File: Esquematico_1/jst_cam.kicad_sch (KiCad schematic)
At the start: 10 parts, among them J1 Screw_Terminal_01x04, J2 Screw_Terminal_01x03, J3 Screw_Terminal_01x06, J4 Screw_Terminal_01x08, J5 USB_C_Receptacle_USB2.0_14P, J6 Screw_Terminal_01x05, J7 Screw_Terminal_01x02, U5 USBLC6-2SC6

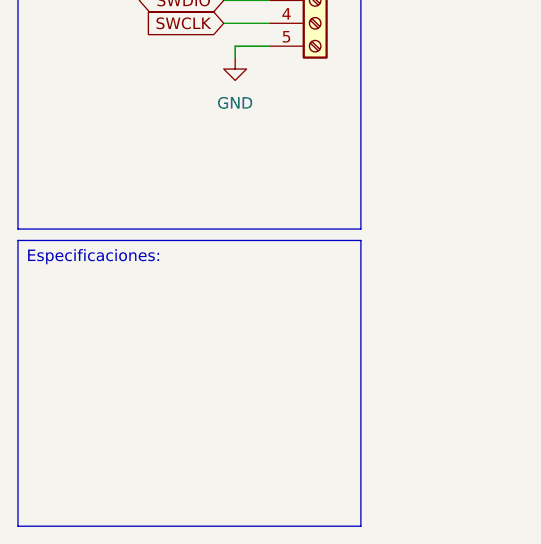
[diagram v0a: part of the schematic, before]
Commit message: Update Circuito de medicion de bateria
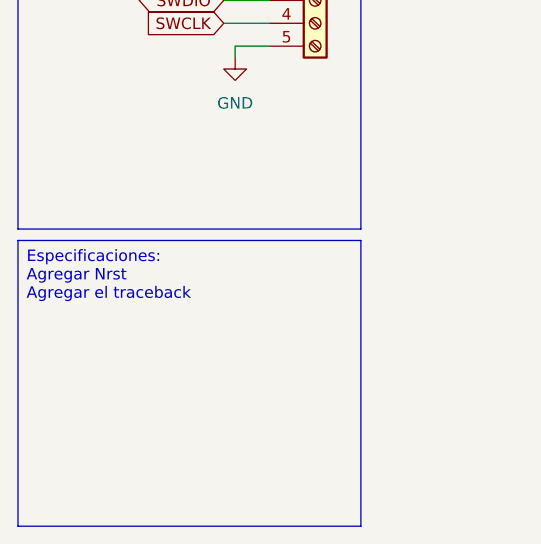
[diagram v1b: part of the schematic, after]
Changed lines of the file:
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@@
 		)
 	)
-	(text_box "Especificaciones: "
+	(text_box "Especificaciones: \nAgregar Nrst\nAgregar el traceback\n"
 		(exclude_from_sim no)
 		(at 24.13 149.86 0)

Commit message: último sensor conectado, y le quité los colores al net_signal xdd
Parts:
- added D3: D_Schottky, symbol Device:D_Schottky
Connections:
- net at J5.A4 (VBUS), J5.A9 (VBUS), J5.B4 (VBUS)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: now also D3.2 (A); no longer U5.5 (VBUS)
- new net: D3.1 (K), U5.5 (VBUS)
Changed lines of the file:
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@@
-	(wire
-		(pts
-			(xy 124.46 113.03) (xy 139.7 113.03)
-		)
-		(stroke
-			(width 0)
-			(type default)
-		)
-	)
 	(wire
 		(pts
@@
 	(wire
 		(pts
+			(xy 137.16 113.03) (xy 139.7 113.03)
+		)
+		(stroke
+			(width 0)
+			(type default)
+		)
+	)
+	(wire
+		(pts
 			(xy 52.07 115.57) (xy 52.07 118.11)
 		)
@@
 		(pts
 			(xy 190.5 46.99) (xy 194.31 46.99)
+		)
+		(stroke
+			(width 0)
+			(type default)
+		)
+	)
+	(wire
+		(pts
+			(xy 124.46 113.03) (xy 129.54 113.03)
 		)
 		(stroke
@@
 					(unit 1)
 				)
+			)
+		)
+	)
+	(symbol
+		(lib_id "Device:D_Schottky")
+		(at 133.35 113.03 180)
+		(unit 1)
+		(exclude_from_sim no)
+		(in_bom yes)
+		(on_board yes)
+		(dnp no)
+		(fields_autoplaced yes)
+		(property "Reference" "D3"
+			(at 133.6675 106.68 0)
+			(effects
+				(font
+					(size 1.27 1.27)
+				)
+			)
+		)
+		(property "Value" "D_Schottky"
+			(at 133.6675 109.22 0)
+			(effects
+				(font
+					(size 1.27 1.27)
+				)
+			)
+		)
+		(property "Footprint" ""
+			(at 133.35 113.03 0)
+			(effects
+				(font
+					(size 1.27 1.27)
+				)
+				(hide yes)
+			)
+		)
+		(property "Datasheet" "~"
+			(at 133.35 113.03 0)
+			(effects
+				(font
+					(size 1.27 1.27)
+				)
+				(hide yes)
+			)
+		)
+		(property "Description" "Schottky diode"
+			(at 133.35 113.03 0)
+			(effects
+				(font
+					(size 1.27 1.27)
+				)
+				(hide yes)
+			)
+		)
+		(pin "1"
+		)
+		(pin "2"
+		)
+		(instances
+			(project ""
+				(path "/de2d80c1-c21c-478d-b724-17659b714c38/457e76de-adfe-4ec5-a818-c5970caa89a7"
+					(reference "D3")
+					(unit 1)
+				)

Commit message: Update llamada
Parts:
- removed J7: Screw_Terminal_01x02, symbol Connector:Screw_Terminal_01x02
- added D4, D5, D6: D_Schottky, symbol Device:D_Schottky
- added JP1, JP2: SolderJumper_2_Open, symbol Jumper:SolderJumper_2_Open
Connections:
- net 5v: now also D4.2 (A), D5.2 (A), D6.2 (A); no longer J1.3 (Pin_3), J2.1 (Pin_1), J3.4 (Pin_4)
- net ESC1: now also J4.1 (Pin_1)
- net ESC2: now also J4.2 (Pin_2)
- net ESC3: now also J4.3 (Pin_3)
- net ESC4: now also J4.4 (Pin_4)
- net TELEM_ESC: now also J4.6 (Pin_6)
- net at J4.5 (Pin_5): now also JP2.1 (A)
- net at J4.7 (Pin_7): now also JP1.1 (A)
- new net: D5.1 (K), J1.3 (Pin_3)
- new net: D6.1 (K), J2.1 (Pin_1)
- new net: D4.1 (K), J3.4 (Pin_4)
- new net CRT: JP2.2 (B)
- new net VCC: JP1.2 (B)
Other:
- moved on the sheet: J4

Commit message: Update Fisubles
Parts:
- added F2, F3: Polyfuse, symbol Device:Polyfuse
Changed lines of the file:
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@@
+	)
+	(symbol
+		(lib_id "Device:Polyfuse")
+		(at 171.45 57.15 0)
+		(unit 1)
+		(exclude_from_sim no)
+		(in_bom yes)
+		(on_board yes)
+		(dnp no)
+		(fields_autoplaced yes)
+		(property "Reference" "F3"
+			(at 173.99 55.8799 0)
+			(effects
+				(font
+					(size 1.27 1.27)
+				)
+				(justify left)
+			)
+		)
+		(property "Value" "Polyfuse"
+			(at 173.99 58.4199 0)
+			(effects
+				(font
+					(size 1.27 1.27)
+				)
+				(justify left)
+			)
+		)
+		(property "Footprint" ""
+			(at 172.72 62.23 0)
+			(effects
+				(font
+					(size 1.27 1.27)
+				)
+				(justify left)
+				(hide yes)
+			)
+		)
+		(property "Datasheet" "~"
+			(at 171.45 57.15 0)
+			(effects
+				(font
+					(size 1.27 1.27)
+				)
+				(hide yes)
+			)
+		)
+		(property "Description" "Resettable fuse, polymeric positive temperature coefficient"
+			(at 171.45 57.15 0)
+			(effects
+				(font
+					(size 1.27 1.27)
+				)
+				(hide yes)
+			)
+		)
+		(pin "2"
+		)
+		(pin "1"
+		)
+		(instances
+			(project "Esquematico_1"
+				(path "/de2d80c1-c21c-478d-b724-17659b714c38/457e76de-adfe-4ec5-a818-c5970caa89a7"
+					(reference "F3")
+					(unit 1)
+				)
+			)
+		)
+	)
+	(symbol
+		(lib_id "Device:Polyfuse")
+		(at 105.41 55.88 0)
+		(unit 1)
+		(exclude_from_sim no)
+		(in_bom yes)
+		(on_board yes)
+		(dnp no)
+		(fields_autoplaced yes)
+		(property "Reference" "F2"
+			(at 107.95 54.6099 0)
+			(effects
+				(font
+					(size 1.27 1.27)
+				)
+				(justify left)
+			)
+		)
+		(property "Value" "Polyfuse"
+			(at 107.95 57.1499 0)
+			(effects
+				(font
+					(size 1.27 1.27)
+				)
+				(justify left)
+			)
+		)
+		(property "Footprint" ""
+			(at 106.68 60.96 0)
+			(effects
+				(font
+					(size 1.27 1.27)
+				)
+				(justify left)
+				(hide yes)
+			)
+		)
+		(property "Datasheet" "~"
+			(at 105.41 55.88 0)
+			(effects
+				(font
+					(size 1.27 1.27)
+				)
+				(hide yes)
+			)
+		)
+		(property "Description" "Resettable fuse, polymeric positive temperature coefficient"
+			(at 105.41 55.88 0)
+			(effects
+				(font
+					(size 1.27 1.27)
+				)
+				(hide yes)
+			)
+		)
+		(pin "2"
+		)
+		(pin "1"
+		)
+		(instances
+			(project "Esquematico_1"
+				(path "/de2d80c1-c21c-478d-b724-17659b714c38/457e76de-adfe-4ec5-a818-c5970caa89a7"
+					(reference "F2")
+					(unit 1)
+				)
+			)
+		)
 	)
 	(symbol

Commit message: Cambio del cristal por n-ésima vez
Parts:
- D3, D4, D5, D6: footprint (none) -> Package_TO_SOT_SMD:SOT-23
- JP1, JP2: footprint (none) -> Jumper:SolderJumper-2_P1.3mm_Open_RoundedPad1.0x1.5mm
- R15, R16: footprint (none) -> Resistor_SMD:R_0805_2012Metric_Pad1.20x1.40mm_HandSolder
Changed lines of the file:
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@@
 			)
 		)
-		(property "Footprint" ""
+		(property "Footprint" "Package_TO_SOT_SMD:SOT-23"
 			(at 182.88 48.26 0)
 			(effects
@@
 			)
 		)
-		(property "Footprint" ""
+		(property "Footprint" "Package_TO_SOT_SMD:SOT-23"
 			(at 116.84 46.99 0)
 			(effects
@@
 			)
 		)
-		(property "Footprint" ""
+		(property "Footprint" "Jumper:SolderJumper-2_P1.3mm_Open_RoundedPad1.0x1.5mm"
 			(at 58.42 50.8 0)
 			(effects
@@
 			)
 		)
-		(property "Footprint" ""
+		(property "Footprint" "Package_TO_SOT_SMD:SOT-23"
 			(at 256.54 40.64 0)
 			(effects
@@
 			)
 		)
-		(property "Footprint" ""
+		(property "Footprint" "Package_TO_SOT_SMD:SOT-23"
 			(at 133.35 113.03 0)
 			(effects
@@
 			)
 		)
-		(property "Footprint" ""
+		(property "Footprint" "Jumper:SolderJumper-2_P1.3mm_Open_RoundedPad1.0x1.5mm"
 			(at 53.34 45.72 0)
 			(effects
@@
 			)
 		)
-		(property "Footprint" ""
+		(property "Footprint" "Resistor_SMD:R_0805_2012Metric_Pad1.20x1.40mm_HandSolder"
 			(at 130.302 148.59 90)
 			(effects
@@
 			)
 		)
-		(property "Footprint" ""
+		(property "Footprint" "Resistor_SMD:R_0805_2012Metric_Pad1.20x1.40mm_HandSolder"
 			(at 123.952 148.59 90)
 			(effects

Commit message: Update polyfuse
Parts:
- added F4, F5: Polyfuse, symbol Device:Polyfuse
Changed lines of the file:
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@@
+	)
+	(symbol
+		(lib_id "Device:Polyfuse")
+		(at 246.38 54.61 0)
+		(unit 1)
+		(exclude_from_sim no)
+		(in_bom yes)
+		(on_board yes)
+		(dnp no)
+		(fields_autoplaced yes)
+		(property "Reference" "F4"
+			(at 248.92 53.3399 0)
+			(effects
+				(font
+					(size 1.27 1.27)
+				)
+				(justify left)
+			)
+		)
+		(property "Value" "Polyfuse"
+			(at 248.92 55.8799 0)
+			(effects
+				(font
+					(size 1.27 1.27)
+				)
+				(justify left)
+			)
+		)
+		(property "Footprint" ""
+			(at 247.65 59.69 0)
+			(effects
+				(font
+					(size 1.27 1.27)
+				)
+				(justify left)
+				(hide yes)
+			)
+		)
+		(property "Datasheet" "~"
+			(at 246.38 54.61 0)
+			(effects
+				(font
+					(size 1.27 1.27)
+				)
+				(hide yes)
+			)
+		)
+		(property "Description" "Resettable fuse, polymeric positive temperature coefficient"
+			(at 246.38 54.61 0)
+			(effects
+				(font
+					(size 1.27 1.27)
+				)
+				(hide yes)
+			)
+		)
+		(pin "2"
+		)
+		(pin "1"
+		)
+		(instances
+			(project "Esquematico_1"
+				(path "/de2d80c1-c21c-478d-b724-17659b714c38/457e76de-adfe-4ec5-a818-c5970caa89a7"
+					(reference "F4")
+					(unit 1)
+				)
+			)
+		)
 	)
 	(symbol
@@
 					(unit 1)
 				)
+			)
+		)
+	)
+	(symbol
+		(lib_id "Device:Polyfuse")
+		(at 149.86 146.05 0)
+		(unit 1)
+		(exclude_from_sim no)
+		(in_bom yes)
+		(on_board yes)
+		(dnp no)
+		(fields_autoplaced yes)
+		(property "Reference" "F5"
+			(at 152.4 144.7799 0)
+			(effects
+				(font
+					(size 1.27 1.27)
+				)
+				(justify left)
+			)
+		)
+		(property "Value" "Polyfuse"
+			(at 152.4 147.3199 0)
+			(effects
+				(font
+					(size 1.27 1.27)
+				)
+				(justify left)
+			)
+		)
+		(property "Footprint" ""
+			(at 151.13 151.13 0)
+			(effects
+				(font
+					(size 1.27 1.27)
+				)
+				(justify left)
+				(hide yes)
+			)
+		)
+		(property "Datasheet" "~"
+			(at 149.86 146.05 0)
+			(effects
+				(font
+					(size 1.27 1.27)
+				)
+				(hide yes)
+			)
+		)
+		(property "Description" "Resettable fuse, polymeric positive temperature coefficient"
+			(at 149.86 146.05 0)
+			(effects
+				(font
+					(size 1.27 1.27)
+				)
+				(hide yes)
+			)
+		)
+		(pin "2"
+		)
+		(pin "1"
+		)
+		(instances
+			(project "Esquematico_1"
+				(path "/de2d80c1-c21c-478d-b724-17659b714c38/457e76de-adfe-4ec5-a818-c5970caa89a7"
+					(reference "F5")
+					(unit 1)
+				)

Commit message: Footprints
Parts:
- F2: value Polyfuse -> 750mA; footprint (none) -> Capacitor_SMD:C_0805_2012Metric_Pad1.18x1.45mm_HandSolder
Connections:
- net 5v: now also F2.1; no longer D4.2 (A)
- net at F2.2: now also D4.2 (A)
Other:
- moved on the sheet: F2
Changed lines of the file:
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@@
+	(wire
+		(pts
+			(xy 102.87 46.99) (xy 104.14 46.99)
+		)
+		(stroke
+			(width 0)
+			(type default)
+		)
+	)
 	(wire
 		(pts
@@
 	(wire
 		(pts
+			(xy 111.76 46.99) (xy 113.03 46.99)
+		)
+		(stroke
+			(width 0)
+			(type default)
+		)
+	)
+	(wire
+		(pts
 			(xy 144.78 128.27) (xy 154.94 128.27)
 		)
@@
 		(pts
 			(xy 119.38 39.37) (xy 123.19 39.37)
-		)
-		(stroke
-			(width 0)
-			(type default)
-		)
-	)
-	(wire
-		(pts
-			(xy 113.03 46.99) (xy 110.49 46.99)
 		)
 		(stroke
@@
 	(symbol
 		(lib_id "Device:Polyfuse")
-		(at 105.41 55.88 0)
+		(at 107.95 46.99 90)
 		(unit 1)
 		(exclude_from_sim no)
@@
 		(on_board yes)
 		(dnp no)
-		(fields_autoplaced yes)
 		(property "Reference" "F2"
-			(at 107.95 54.6099 0)
-			(effects
-				(font
-					(size 1.27 1.27)
-				)
-				(justify left)
-			)
-		)
-		(property "Value" "Polyfuse"
-			(at 107.95 57.1499 0)
-			(effects
-				(font
-					(size 1.27 1.27)
-				)
-				(justify left)
-			)
-		)
-		(property "Footprint" ""
-			(at 106.68 60.96 0)
+			(at 103.632 50.8 90)
+			(effects
+				(font
+					(size 1.27 1.27)
+				)
+			)
+		)
+		(property "Value" "750mA"
+			(at 103.632 53.34 90)
+			(effects
+				(font
+					(size 1.27 1.27)
+				)
+			)
+		)
+		(property "Footprint" "Capacitor_SMD:C_0805_2012Metric_Pad1.18x1.45mm_HandSolder"
+			(at 113.03 45.72 0)
 			(effects
 				(font
@@
 		)
 		(property "Datasheet" "~"
-			(at 105.41 55.88 0)
+			(at 107.95 46.99 0)
 			(effects
 				(font
@@
 		)
 		(property "Description" "Resettable fuse, polymeric positive temperature coefficient"
-			(at 105.41 55.88 0)
+			(at 107.95 46.99 0)
 			(effects
 				(font
@@
 	(symbol
 		(lib_id "power:+3.3V")
-		(at 110.49 46.99 90)
+		(at 102.87 46.99 90)
 		(unit 1)
 		(exclude_from_sim no)
@@
 		(on_board yes)
 		(dnp no)
-		(fields_autoplaced yes)
 		(property "Reference" "#PWR046"
-			(at 114.3 46.99 0)
+			(at 106.68 46.99 0)
 			(effects
 				(font
@@
 		)
 		(property "Value" "5v"
-			(at 106.68 46.9899 90)
+			(at 101.854 43.942 90)
 			(effects
 				(font
@@
 		)
 		(property "Footprint" ""
-			(at 110.49 46.99 0)
+			(at 102.87 46.99 0)
 			(effects
 				(font
@@
 		)
 		(property "Datasheet" ""
-			(at 110.49 46.99 0)
+			(at 102.87 46.99 0)
 			(effects
 				(font
@@
 		)
 		(property "Description" "Power symbol creates a global label with name \"+3.3V\""
-			(at 110.49 46.99 0)
-			(effects
-				(font
+			(at 102.87 46.99 0)
+			(effects
+				(font

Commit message: USB 16 Pin
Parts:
- removed J5: USB_C_Receptacle_USB2.0_14P, symbol Connector:USB_C_Receptacle_USB2.0_14P
- added J7: USB_C_Receptacle_USB2.0_16P, symbol Connector:USB_C_Receptacle_USB2.0_16P
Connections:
- net CC1: now also J7.A5 (CC1)
- net CC2: now also J7.B5 (CC2)
- net GND: now also J7.A1 (GND), J7.A12 (GND), J7.B1 (GND), J7.B12 (GND), J7.S1 (SHIELD)
- net at D3.2 (A): now also J7.A4 (VBUS), J7.A9 (VBUS), J7.B4 (VBUS), J7.B9 (VBUS)
- net at U5.3 (I/O2): now also J7.A6 (D+), J7.B6 (D+)
- net at U5.1 (I/O1): now also J7.A7 (D-), J7.B7 (D-)
- no-connect marks 0 -> 2
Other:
- moved on the sheet: R15, R16
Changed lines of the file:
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@@
 	)
 	(junction
-		(at 125.73 153.67)
+		(at 128.27 153.67)
 		(diameter 0)
 		(color 0 0 0 0)
@@
 		(color 0 0 0 0)
 	)
+	(no_connect
+		(at 124.46 143.51)
+	)
+	(no_connect
+		(at 124.46 140.97)
+	)
 	(wire
 		(pts
@@
 	(wire
 		(pts
-			(xy 125.73 140.97) (xy 125.73 144.78)
+			(xy 128.27 140.97) (xy 128.27 144.78)
 		)
 		(stroke
@@
 	(wire
 		(pts
-			(xy 132.08 152.4) (xy 132.08 153.67)
+			(xy 134.62 152.4) (xy 134.62 153.67)
 		)
 		(stroke
@@
 	(wire
 		(pts
-			(xy 132.08 140.97) (xy 132.08 144.78)
+			(xy 134.62 140.97) (xy 134.62 144.78)
 		)
 		(stroke
@@
 	(wire
 		(pts
-			(xy 125.73 152.4) (xy 125.73 153.67)
+			(xy 128.27 152.4) (xy 128.27 153.67)
 		)
 		(stroke
@@
 	(wire
 		(pts
-			(xy 125.73 153.67) (xy 132.08 153.67)
+			(xy 128.27 153.67) (xy 134.62 153.67)
 		)
 		(stroke
@@
 	)
 	(label "CC1"
-		(at 125.73 140.97 90)
+		(at 128.27 140.97 90)
 		(effects
 			(font
@@
 	)
 	(label "CC2"
-		(at 132.08 140.97 90)
+		(at 134.62 140.97 90)
 		(effects
 			(font
@@
 	)
 	(symbol
-		(lib_id "Connector:USB_C_Receptacle_USB2.0_14P")
-		(at 109.22 128.27 0)
-		(unit 1)
-		(exclude_from_sim no)
-		(in_bom yes)
-		(on_board yes)
-		(dnp no)
-		(property "Reference" "J5"
-			(at 109.22 105.41 0)
-			(effects
-				(font
-					(size 1.27 1.27)
-				)
-			)
-		)
-		(property "Value" "USB_C_Receptacle_USB2.0_14P"
-			(at 109.22 107.95 0)
-			(effects
-				(font
-					(size 1.27 1.27)
-				)
-			)
-		)
-		(property "Footprint" ""
-			(at 113.03 128.27 0)
-			(effects
-				(font
-					(size 1.27 1.27)
-				)
-				(hide yes)
-			)
-		)
-		(property "Datasheet" "https://www.usb.org/sites/default/files/documents/usb_type-c.zip"
-			(at 113.03 128.27 0)
-			(effects
-				(font
-					(size 1.27 1.27)
-				)
-				(hide yes)
-			)
-		)
-		(property "Description" "USB 2.0-only 14P Type-C Receptacle connector"
-			(at 109.22 128.27 0)
-			(effects
-				(font
-					(size 1.27 1.27)
-				)
-				(hide yes)
-			)
-		)
-		(pin "B7"
-		)
-		(pin "B5"
-		)
-		(pin "B6"
-		)
-		(pin "A6"
-		)
-		(pin "B4"
-		)
-		(pin "A7"
-		)
-		(pin "S1"
-		)
-		(pin "B9"
-		)
-		(pin "A5"
-		)
-		(pin "A1"
-		)
-		(pin "A12"
-		)
-		(pin "B1"
-		)
-		(pin "B12"
-		)
-		(pin "A4"
-		)
-		(pin "A9"
-		)
-		(instances
-			(project "Esquematico_1"
-				(path "/de2d80c1-c21c-478d-b724-17659b714c38/457e76de-adfe-4ec5-a818-c5970caa89a7"
-					(reference "J5")
-					(unit 1)
-				)
-			)
-		)
-	)
-	(symbol
 		(lib_id "power:GND")
 		(at 66.04 54.61 0)
@@
 	)
 	(symbol
+		(lib_id "Connector:USB_C_Receptacle_USB2.0_16P")
+		(at 109.22 128.27 0)
+		(unit 1)
+		(exclude_from_sim no)
+		(in_bom yes)
+		(on_board yes)
+		(dnp no)
+		(fields_autoplaced yes)
+		(property "Reference" "J7"
+			(at 109.22 105.41 0)
+			(effects
+				(font
+					(size 1.27 1.27)
+				)
+			)
+		)
+		(property "Value" "USB_C_Receptacle_USB2.0_16P"
+			(at 109.22 107.95 0)
+			(effects
+				(font
+					(size 1.27 1.27)
+				)
+			)
+		)
+		(property "Footprint" ""
+			(at 113.03 128.27 0)
+			(effects
+				(font
+					(size 1.27 1.27)
+				)
+				(hide yes)
+			)
+		)
+		(property "Datasheet" "https://www.usb.org/sites/default/files/documents/usb_type-c.zip"
+			(at 113.03 128.27 0)
+			(effects
+				(font
+					(size 1.27 1.27)
+				)
+				(hide yes)
+			)
+		)
+		(property "Description" "USB 2.0-only 16P Type-C Receptacle connector"
+			(at 109.22 128.27 0)
+			(effects
+				(font
+					(size 1.27 1.27)
+				)
+				(hide yes)
+			)
+		)
+		(pin "B6"
+		)
+		(pin "B4"
+		)
+		(pin "A7"
+		)
+		(pin "A5"
+		)
+		(pin "A1"
+		)
+		(pin "A12"
+		)
+		(pin "A9"
+		)
+		(pin "S1"
+		)
+		(pin "A4"
+		)
+		(pin "B12"
+		)
+		(pin "B1"
+		)
+		(pin "B7"
+		)
+		(pin "A6"
+		)
+		(pin "B9"
+		)
+		(pin "B8"
+		)
+		(pin "B5"
+		)
+		(pin "A8"
+		)
+		(instances
+			(project ""
+				(path "/de2d80c1-c21c-478d-b724-17659b714c38/457e76de-adfe-4ec5-a818-c5970caa89a7"
+					(reference "J7")
+					(unit 1)
+				)
+			)
+		)
+	)
+	(symbol
 		(lib_id "Device:D_Schottky")
 		(at 133.35 113.03 180)
@@
 	(symbol
 		(lib_id "Device:R")
-		(at 132.08 148.59 0)
+		(at 134.62 148.59 0)
 		(unit 1)
 		(exclude_from_sim no)
@@
 		(fields_autoplaced yes)
 		(property "Reference" "R16"
-			(at 134.62 147.3199 0)
+			(at 137.16 147.3199 0)
 			(effects
 				(font
@@
 		)
 		(property "Value" "5k1"
-			(at 134.62 149.8599 0)
+			(at 137.16 149.8599 0)
 			(effects
 				(font
@@
 		)
 		(property "Footprint" "Resistor_SMD:R_0805_2012Metric_Pad1.20x1.40mm_HandSolder"
-			(at 130.302 148.59 90)
+			(at 132.842 148.59 90)
 			(effects
 				(font
@@
 		)
 		(property "Datasheet" "~"
-			(at 132.08 148.59 0)
+			(at 134.62 148.59 0)
 			(effects
 				(font
@@
 		)
 		(property "Description" "Resistor"
-			(at 132.08 148.59 0)
+			(at 134.62 148.59 0)
 			(effects
 				(font
@@
 	(symbol
 		(lib_id "power:GND")
-		(at 125.73 153.67 0)
+		(at 128.27 153.67 0)
 		(unit 1)
 		(exclude_from_sim no)
@@
 		(fields_autoplaced yes)
 		(property "Reference" "#PWR043"
-			(at 125.73 160.02 0)
+			(at 128.27 160.02 0)
 			(effects
 				(font
@@
 		)
 		(property "Value" "GND"
-			(at 125.73 158.75 0)
+			(at 128.27 158.75 0)
 			(effects
 				(font
@@
 		)
 		(property "Footprint" ""
-			(at 125.73 153.67 0)
+			(at 128.27 153.67 0)
 			(effects
 				(font
@@
 		)
 		(property "Datasheet" ""
-			(at 125.73 153.67 0)
+			(at 128.27 153.67 0)
 			(effects
 				(font
@@
 		)
 		(property "Description" "Power symbol creates a global label with name \"GND\" , ground"
-			(at 125.73 153.67 0)
+			(at 128.27 153.67 0)
 			(effects
 				(font
@@
 	(symbol
 		(lib_id "Device:R")
-		(at 125.73 148.59 0)
+		(at 128.27 148.59 0)
 		(unit 1)
 		(exclude_from_sim no)
@@
 		(dnp no)
 		(property "Reference" "R15"
-			(at 120.142 147.066 0)
+			(at 122.682 147.066 0)
 			(effects
 				(font
@@
 		)
 		(property "Value" "5k1"
-			(at 118.364 149.606 0)
+			(at 120.904 149.606 0)
 			(effects
 				(font
@@
 		)
 		(property "Footprint" "Resistor_SMD:R_0805_2012Metric_Pad1.20x1.40mm_HandSolder"
-			(at 123.952 148.59 90)
+			(at 126.492 148.59 90)
 			(effects
 				(font
@@
 		)
 		(property "Datasheet" "~"
-			(at 125.73 148.59 0)
+			(at 128.27 148.59 0)
 			(effects
 				(font
@@
 		)
 		(property "Description" "Resistor"
-			(at 125.73 148.59 0)
+			(at 128.27 148.59 0)
 			(effects
 				(font
